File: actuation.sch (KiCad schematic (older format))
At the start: 4 parts, among them J14 Fan, K1 Songle-SRD, K2 Songle-SRD, U4 ULN2803A

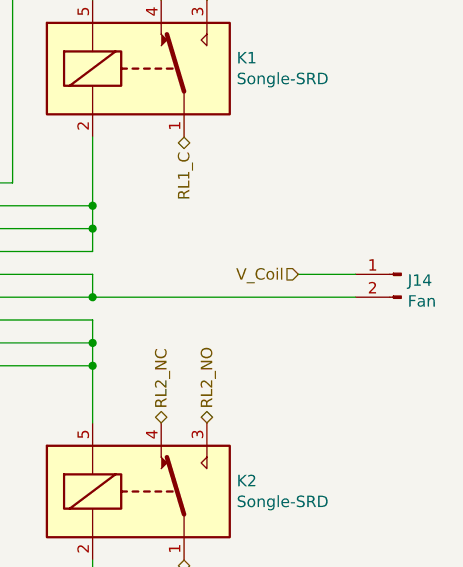
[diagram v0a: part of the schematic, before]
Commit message: Screw connectors footprint changed to 2.54mm ones and relayout done for all terminal blocks
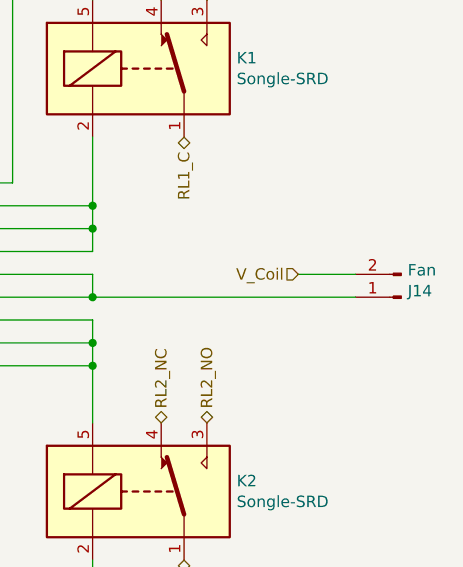
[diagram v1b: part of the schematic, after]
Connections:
- net V_Coil: now also J14.2 (Pin_2); no longer J14.1 (Pin_1)
- net at U4.14 (O5), U4.15 (O4): now also J14.1 (Pin_1); no longer J14.2 (Pin_2)
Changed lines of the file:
@@
 L Connector:Conn_01x02_Male J14
 U 1 1 5BB0A132
-P 6700 2750
-F 0 "J14" H 6672 2723 50  0000 R CNN
-F 1 "Fan" H 6672 2632 50  0000 R CNN
-F 2 "Connector_JST:JST_EH_B02B-EH-A_1x02_P2.50mm_Vertical" H 6700 2750 50  0001 C CNN
-F 3 "~" H 6700 2750 50  0001 C CNN
-	1    6700 2750
-	-1   0    0    -1
+P 6700 2850
+F 0 "J14" H 6672 2823 50  0000 R CNN
+F 1 "Fan" H 6672 2732 50  0000 R CNN
+F 2 "Connector_JST:JST_EH_B02B-EH-A_1x02_P2.50mm_Vertical" H 6700 2850 50  0001 C CNN
+F 3 "~" H 6700 2850 50  0001 C CNN
+	1    6700 2850
+	-1   0    0    1
 $EndComp
 Wire Wire Line
